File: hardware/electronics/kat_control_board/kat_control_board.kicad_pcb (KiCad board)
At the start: 4 copper layers, 84.2 x 173.5 mm, 146 parts, among them J1 USB_C_Receptacle_USB2.0, J10 Conn_01x04, J11 Conn_01x04, J12 Conn_01x04, J13 Conn_01x04, J14 Conn_01x04, J15 Conn_01x04, J16 Conn_01x04, J17 Conn_01x02, J18 Conn_01x04, J19 Conn_01x04, J2 Conn_01x04, J20 Conn_01x02, J21 Conn_01x02, J22 Conn_01x02, J23 Conn_01x02, J24 Conn_01x02, J25 Conn_01x02, J26 Conn_01x02, J27 Conn_01x02, J28 Conn_01x04, J29 Conn_02x30_Odd_Even, J3 Conn_01x04, J30 Conn_02x30_Odd_Even, J31 Conn_02x30_Odd_Even, J32 Conn_02x30_Odd_Even, J33 Conn_01x03, J4 Conn_01x04, J5 Conn_01x04, J6 Conn_01x04, J7 Conn_01x04, J8 Conn_01x04, J9 Conn_01x04, Q1 AO3400A, Q2 AO3400A, Q3 AO3400A, Q4 AO3400A, Q5 AO3400A, SW1 SW_SPST, SW2 SW_SPST, U1 RP2040, U10 SRV05-4, U11 SRV05-4, U12 SRV05-4, U13 SRV05-4, U2 W25Q128JVS, U3 SN74HC4851, U4 74HCT541, U5 SRV05-4, U6 SIC431, U7 XC6206PxxxMR, U8 74HCT541, U9 SRV05-4, Y1 12MHz

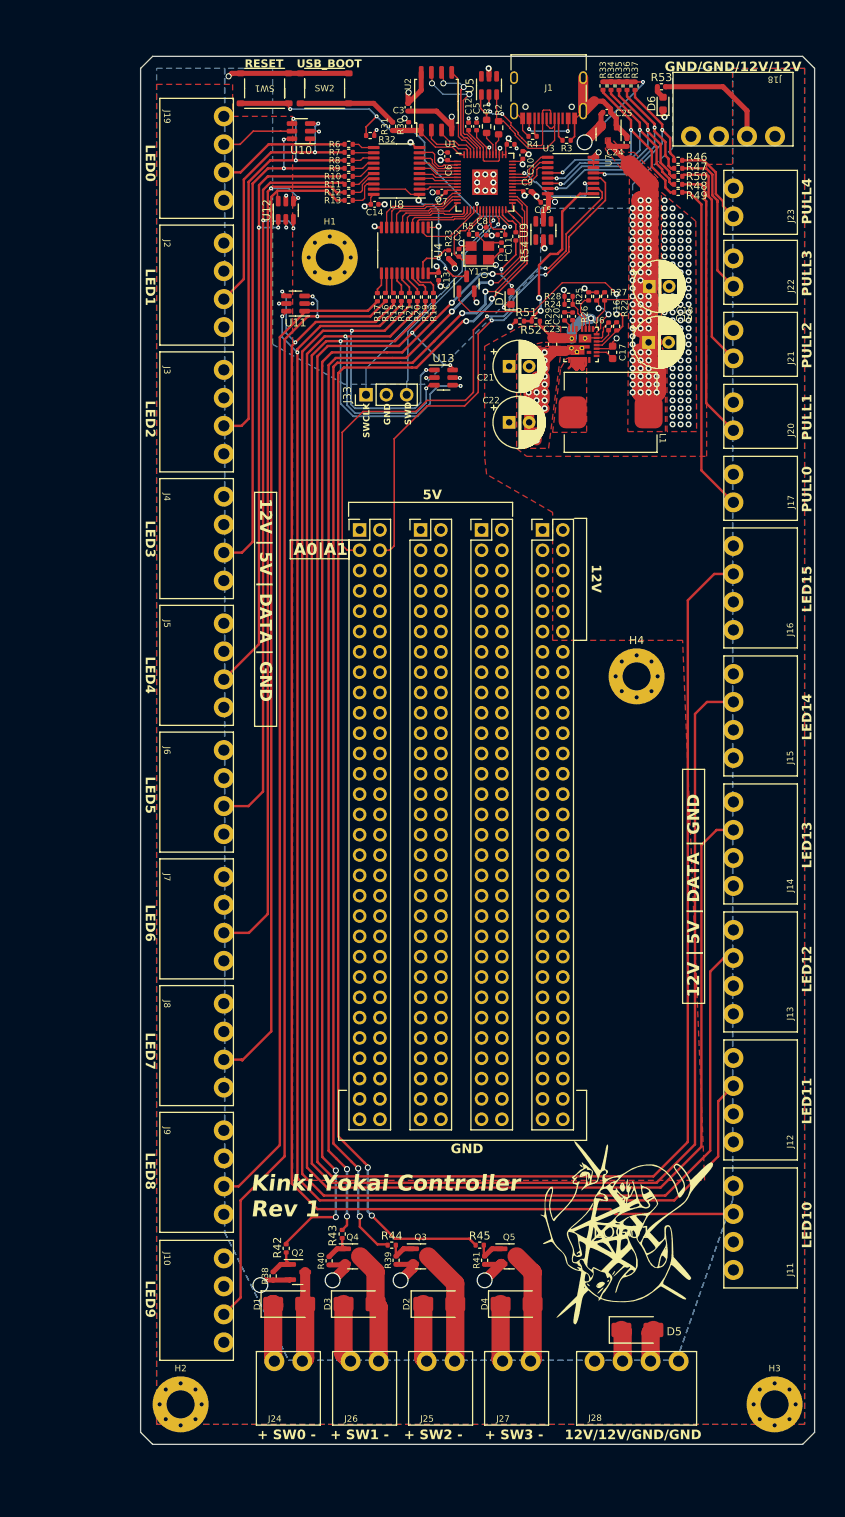
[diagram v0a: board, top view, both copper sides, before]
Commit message: Added test firmware
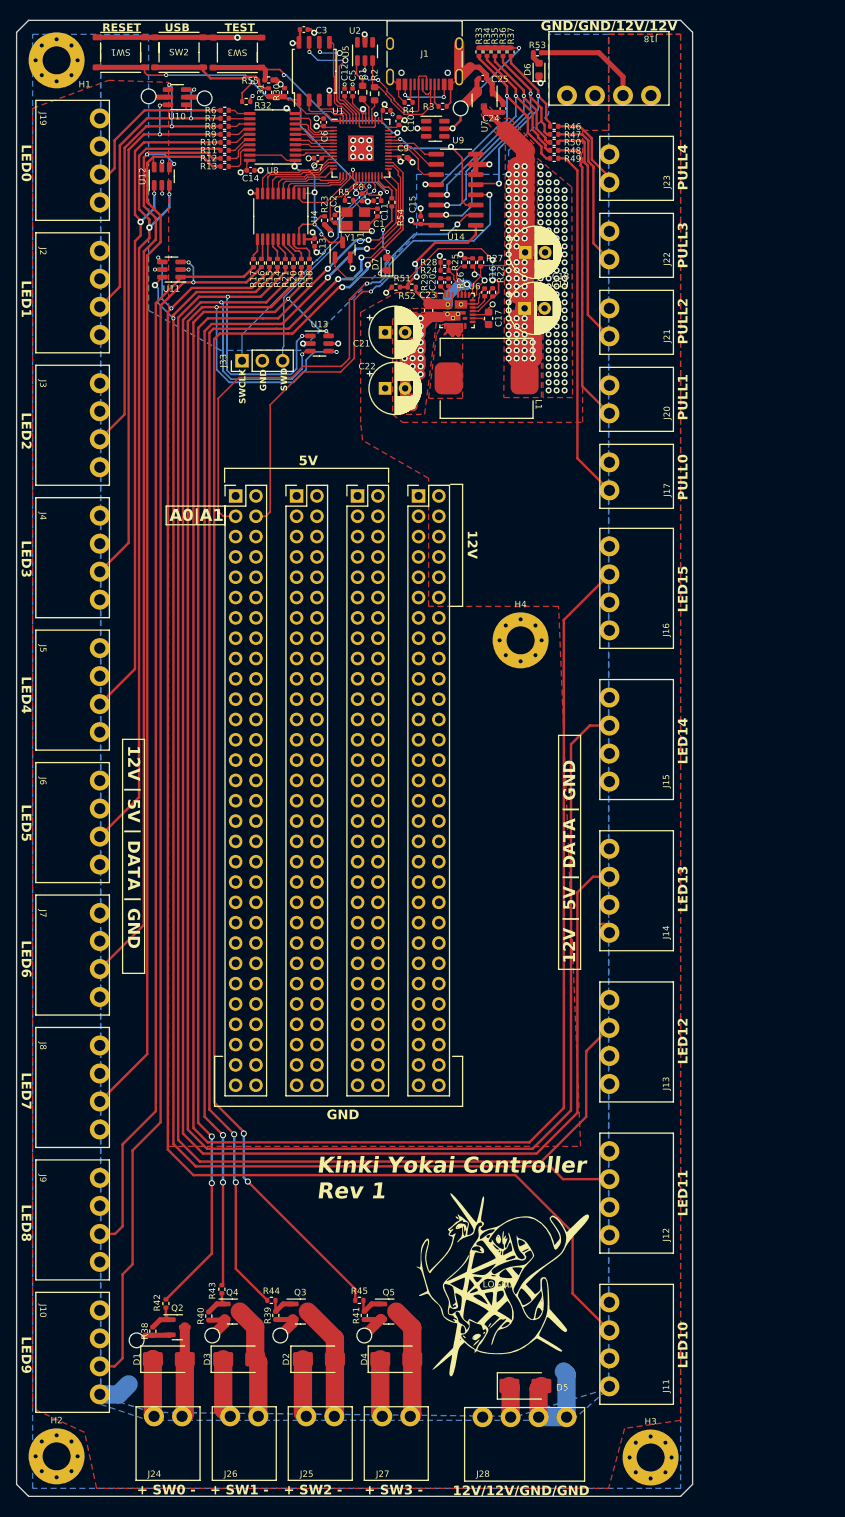
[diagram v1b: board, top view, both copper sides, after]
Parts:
- removed U3: SN74HC4851, Package_SO:TSSOP-16_4.4x5mm_P0.65mm
- added R55: 10kR, Resistor_SMD:R_0402_1005Metric, F.Cu at (44.5, 19.9)
- added SW3: SW_SPST, M_SW:TS-1187A-B-A-B, F.Cu at (40.6, 16.5)
- added U14: CD4051B, Package_SO:SOIC-16_3.9x9.9mm_P1.27mm, F.Cu at (67.9, 33.7)
- moved H1 42.1 mm to (18.0, 17.5)
- moved J11 21.3 mm to (87.1, 178.0)
- moved J12 19.4 mm to (87.1, 159.1)
- moved SW2 18.7 mm to (33.3, 16.5)
- moved SW1 18.6 mm to (26.0, 16.5)
- moved U9 18.6 mm to (65.3, 26.1), turned to 0 degrees
- moved J13 17.8 mm to (87.1, 140.2)
- moved H3 16.9 mm to (92.2, 192.1)
- moved H2 16.8 mm to (18.0, 192.0)
- moved J10 16.8 mm to (23.4, 179.0)
- moved LOGO1 16.8 mm to (73.2, 170.5)
- moved J9 16.6 mm to (23.4, 162.4)
- moved J14 16.6 mm to (87.1, 121.3)
- moved D1 16.5 mm to (32.0, 179.9)
- moved Q2 16.5 mm to (33.1, 175.9)
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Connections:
- U1 pad 39: unconnected-(U1-GPIO27_ADC1-Pad39) -> /TEST
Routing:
- net /TEST: track 0.00 -> 29.3 mm, vias 0 -> 2
- net GND: track 138.5 -> 154.8 mm, vias 155 -> 157
- net /LED12: track 223.5 -> 209.8 mm
- net /LED10: track 184.5 -> 196.8 mm
- net /LED9: track 143.4 -> 155.2 mm
- net /SW1: track 146.6 -> 157.5 mm
- net /SW2: track 152.3 -> 162.9 mm
- net /LED8: track 124.7 -> 134.9 mm
- net /LED13: track 236.3 -> 226.2 mm
- net /LED4: track 78.2 -> 88.0 mm
- net /LED7: track 123.1 -> 132.5 mm
- net /LED11: track 191.1 -> 182.1 mm
- net /SW0: track 152.4 -> 161.4 mm
- net /LED6: track 111.6 -> 119.8 mm
- net /LED5: track 97.0 -> 105.1 mm
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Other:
- board size 84.2 x 173.5 mm -> 84.5 x 184.5 mm
- board text added: "TEST"
- board text added: "USB"
- board text removed: "USB_BOOT"
